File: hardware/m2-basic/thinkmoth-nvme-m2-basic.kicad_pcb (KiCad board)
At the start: 4 copper layers, 31 x 68.4 mm, 24 parts, among them J2 ExpressCard, J3 MDT180M03001, U1 GL823K-HCY04

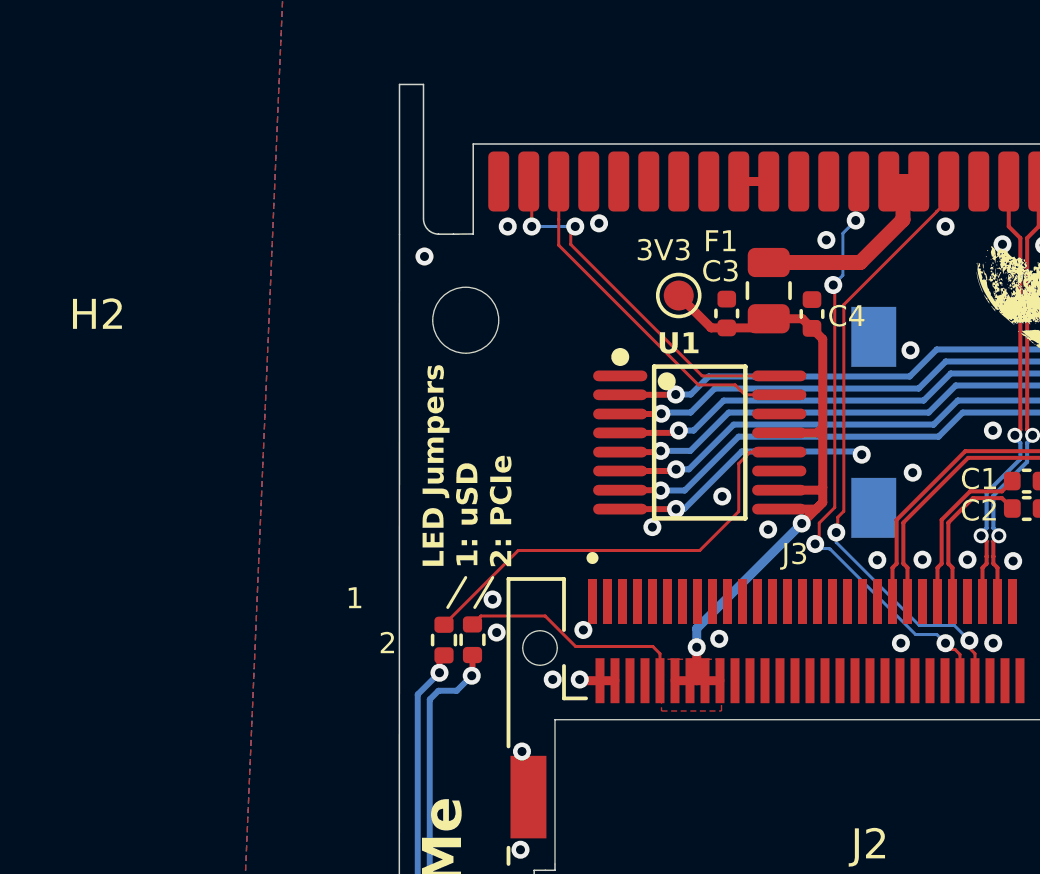
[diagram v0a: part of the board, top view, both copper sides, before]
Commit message: m.2-basic: minor layout tweaks, schem update
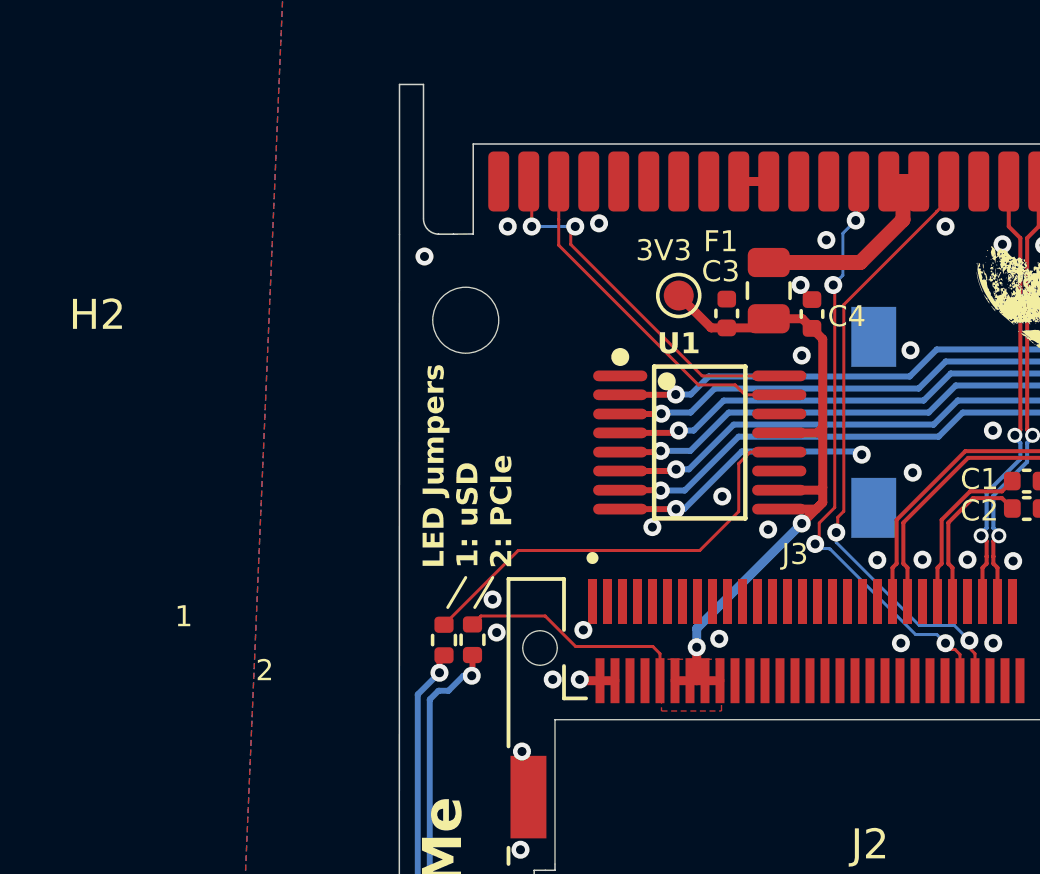
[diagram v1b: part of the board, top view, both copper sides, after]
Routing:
- net PERST: track 18.6 -> 20.0 mm
- net GND: vias 40 -> 42
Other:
- board text added: ":3"
- board text added: "break"
- board text added: "me!"
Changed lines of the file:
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@@
 		(tags "resistor")
 		(property "Reference" "1"
-			(at 1.385001 -2.975 0)
+			(at 0.785001 -8.675 0)
 			(layer "F.SilkS")
 			(effects
@@
 			)
 		)
+		(model "/home/moth/Downloads/m-2_2242_b-m-1.snapshot.3/2242_B_M.step"
+			(hide yes)
+			(offset
+				(xyz 0 -3.5 0)
+			)
+			(scale
+				(xyz 1 1 1)
+			)
+			(rotate
+				(xyz -0 -0 90)
+			)
+		)
+		(model "/home/moth/Downloads/3D Model - MT320, M.2 2230, Key E, SDIO (453-00178)/3D Model - MT320, M.2 2230, Key E, SDIO (453-00178).STEP"
+			(hide yes)
+			(offset
+				(xyz 5.5 -24.3 -24.5)
+			)
+			(scale
+				(xyz 1 1 1)
+			)
+			(rotate
+				(xyz -0 180 -180)
+			)
+		)
 	)
 	(footprint "MountingHole:MountingHole_2.2mm_M2"
@@
 		(tags "resistor")
 		(property "Reference" "2"
-			(at -0.125 -2.825 0)
+			(at -1.025 -6.925 0)
 			(layer "F.SilkS")
 			(effects
@@
 		)
 	)
+	(gr_text "break"
+		(at 83.5 103.2 0)
+		(layer "B.SilkS")
+		(effects
+			(font
+				(size 1 1)
+				(thickness 0.25)
+				(bold yes)
+			)
+			(justify left bottom mirror)
+		)
+	)
+	(gr_text "me!"
+		(at 71.2 103.2 0)
+		(layer "B.SilkS")
+		(effects
+			(font
+				(size 1 1)
+				(thickness 0.25)
+				(bold yes)
+			)
+			(justify left bottom mirror)
+		)
+	)
+	(gr_text ":3"
+		(at 89.3 61.5 270)
+		(layer "B.SilkS")
+		(effects
+			(font
+				(size 1 1)
+				(thickness 0.25)
+				(bold yes)
+			)
+			(justify left bottom mirror)
+		)
+	)
 	(segment
 		(start 78.625 66.5)
@@
 	)
 	(via
+		(at 73.56117 55.95)
+		(size 0.6)
+		(drill 0.3)
+		(layers "F.Cu" "B.Cu")
+		(free yes)
+		(net 3)
+	)
+	(via
 		(at 80.646943 65.152216)
 		(size 0.6)
@@
 	)
 	(via
+		(at 73.6 58.3)
+		(size 0.6)
+		(drill 0.3)
+		(layers "F.Cu" "B.Cu")
+		(free yes)
+		(net 3)
+	)
+	(via
 		(at 87.375 74.85)
 		(size 0.6)
@@
 		(net 15)
 	)
+	(segment
+		(start 75.4 53.8)
+		(end 75.5 53.7)
+		(width 0.1)
+		(layer "F.Cu")
+		(net 15)
+	)
+	(segment
+		(start 75.5 53.7)
+		(end 75.5 52.5)
+		(width 0.1)
+		(layer "F.Cu")
+		(net 15)
+	)
 	(via
 		(at 74.047681 64.583083)
@@
 	)
 	(segment
-		(start 61.201 69.7661)
-		(end 61.4911 69.476)
+		(start 63.3 113.1)
+		(end 64.077473 112.322527)
 		(width 0.2)
 		(layer "B.Cu")
@@
 	)
 	(segment
-		(start 63.3 108.8)
-		(end 61.4 108.8)
+		(start 61.4 108.8)
+		(end 61.201 108.601)
 		(width 0.2)
 		(layer "B.Cu")
@@
 	)
 	(segment
-		(start 61.4 113.85)
-		(end 61.4 113.7)
+		(start 62 113.1)
+		(end 63.3 113.1)
 		(width 0.2)
 		(layer "B.Cu")
@@
 	)
 	(segment
-		(start 64.076562 109.576562)
-		(end 63.3 108.8)
+		(start 61.4 113.7)
+		(end 62 113.1)
+		(width 0.2)
+		(layer "B.Cu")
+		(net 71)
+	)
+	(segment
+		(start 61.4 113.85)
+		(end 61.4 113.7)
 		(width 0.2)
 		(layer "B.Cu")
@@
 	)
 	(segment
-		(start 62.099 69.476)
+		(start 62.325 68.975)
 		(end 62.6 68.975)
 		(width 0.2)
@@
 	)
 	(segment
-		(start 61.4 113.7)
-		(end 62 113.1)
+		(start 61.4911 69.476)
+		(end 61.824 69.476)
 		(width 0.2)
 		(layer "B.Cu")
@@
 	)
 	(segment
-		(start 62 113.1)
-		(end 63.3 113.1)
+		(start 63.3 108.8)
+		(end 61.4 108.8)
 		(width 0.2)
 		(layer "B.Cu")
@@
 	)
 	(segment
-		(start 64.077473 112.322527)
-		(end 64.077473 111.477473)
+		(start 61.201 108.601)
+		(end 61.201 69.7661)
 		(width 0.2)
 		(layer "B.Cu")
@@
 	)
 	(segment
-		(start 61.4911 69.476)
-		(end 62.099 69.476)
+		(start 64.077473 112.322527)
+		(end 64.077473 111.477473)
 		(width 0.2)
 		(layer "B.Cu")
@@
 	)
 	(segment
-		(start 61.201 108.601)
-		(end 61.201 69.7661)
+		(start 61.201 69.7661)
+		(end 61.4911 69.476)
 		(width 0.2)
 		(layer "B.Cu")
@@
 	)
 	(segment
-		(start 61.4 108.8)
-		(end 61.201 108.601)
+		(start 64.076562 109.576562)
+		(end 63.3 108.8)
 		(width 0.2)
 		(layer "B.Cu")
@@
 	)
 	(segment
-		(start 63.3 113.1)
-		(end 64.077473 112.322527)
+		(start 61.824 69.476)
+		(end 62.325 68.975)
 		(width 0.2)
 		(layer "B.Cu")

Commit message: updates for prototype run
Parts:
- J2: renamed from J3; footprint MDT180M03001_2:AMPHENOL_MDT180M03001 -> thinkmoth:AMPHENOL_MDT180M03001
- renumbered C3 to C1, C4 to C2, C1 to C3, C2 to C4, J2 to J1, Card1 to J3, 1 to JM1, 2 to JM2, R5 to R1, R6 to R2
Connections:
- net PCIe_LED renamed LED_PCIe
- net SD_LED renamed LED_SD
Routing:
- net GND: track 0.00 -> 12.9 mm, vias 42 -> 35
- added copper zone on In2.Cu, net GND
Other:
- board text added: ":("
- board text added: "M.2 2230 + 2242 V0.1"
- board text added: "TM-NVME-EC34"
- board text added: "huge thanks to: wificable 0xarya ambraglow HackMods everyone else :3"
- board text removed: "M.2 2230 + 2242"

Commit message: minor tweaks
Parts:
- J3: value TF-001B -> TF-009; footprint SOFNG-TF-001B:TF-SMD_TF-001B -> SOFNG-TF-009:TF-SMD_TF-009
- moved J3 1.22 mm to (82.5, 61.7), turned to 90 degrees
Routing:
- net SD_DAT3: track 20.8 -> 23.9 mm
- net SD_CLK: track 19.9 -> 22.7 mm
- net SD_CMD: track 20.7 -> 23.5 mm
- net SD_DAT1: track 19.7 -> 22.4 mm
- net SD_DAT0: track 19.6 -> 22.3 mm
- net SD_DAT2: track 22.4 -> 24.3 mm
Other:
- board text added: "Prototype"
- board text added: "huge thanks to: wificable 0xarya ambraglow HackMods!!! everyone else :3"
- board text removed: "TM-NVME-EC34"
- board text removed: "huge thanks to: wificable 0xarya ambraglow HackMods everyone else :3"
